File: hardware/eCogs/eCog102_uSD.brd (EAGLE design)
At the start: 47.5 x 28 mm, 7 parts

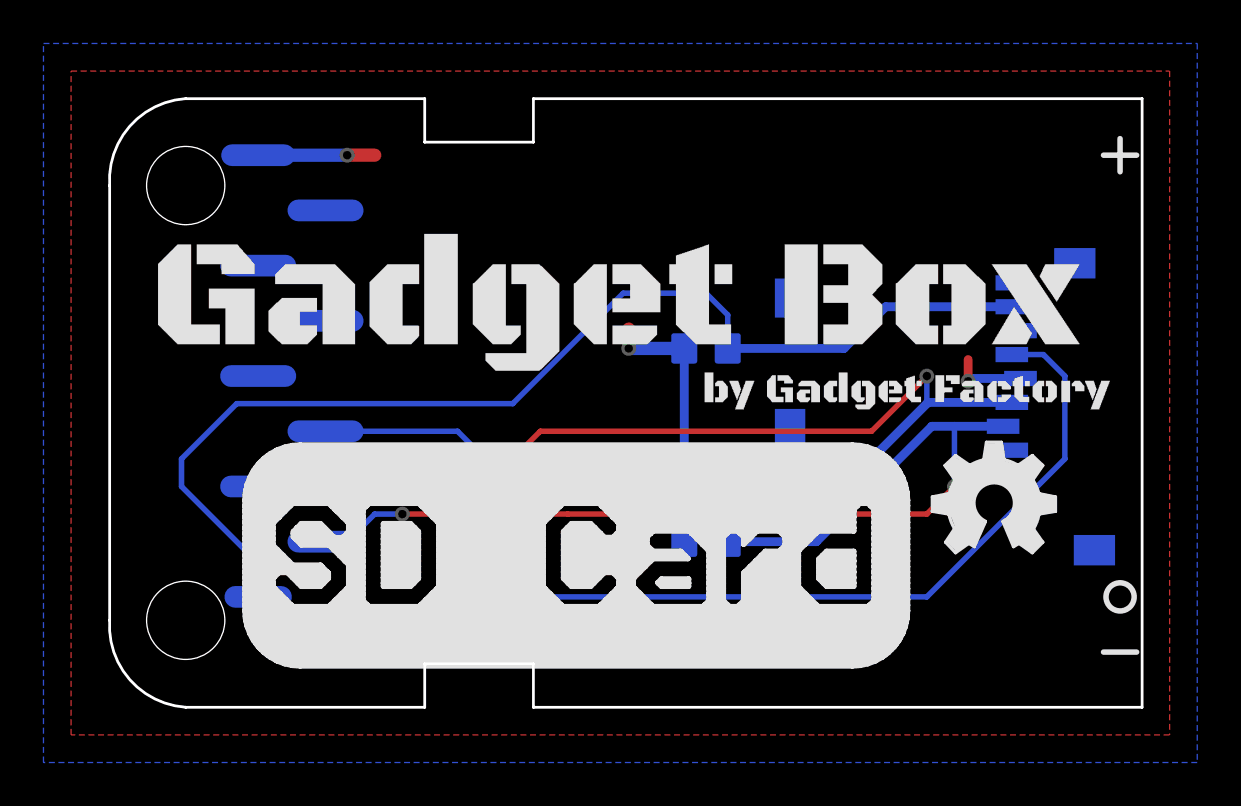
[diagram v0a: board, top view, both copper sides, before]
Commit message: Update eCogs to through hole
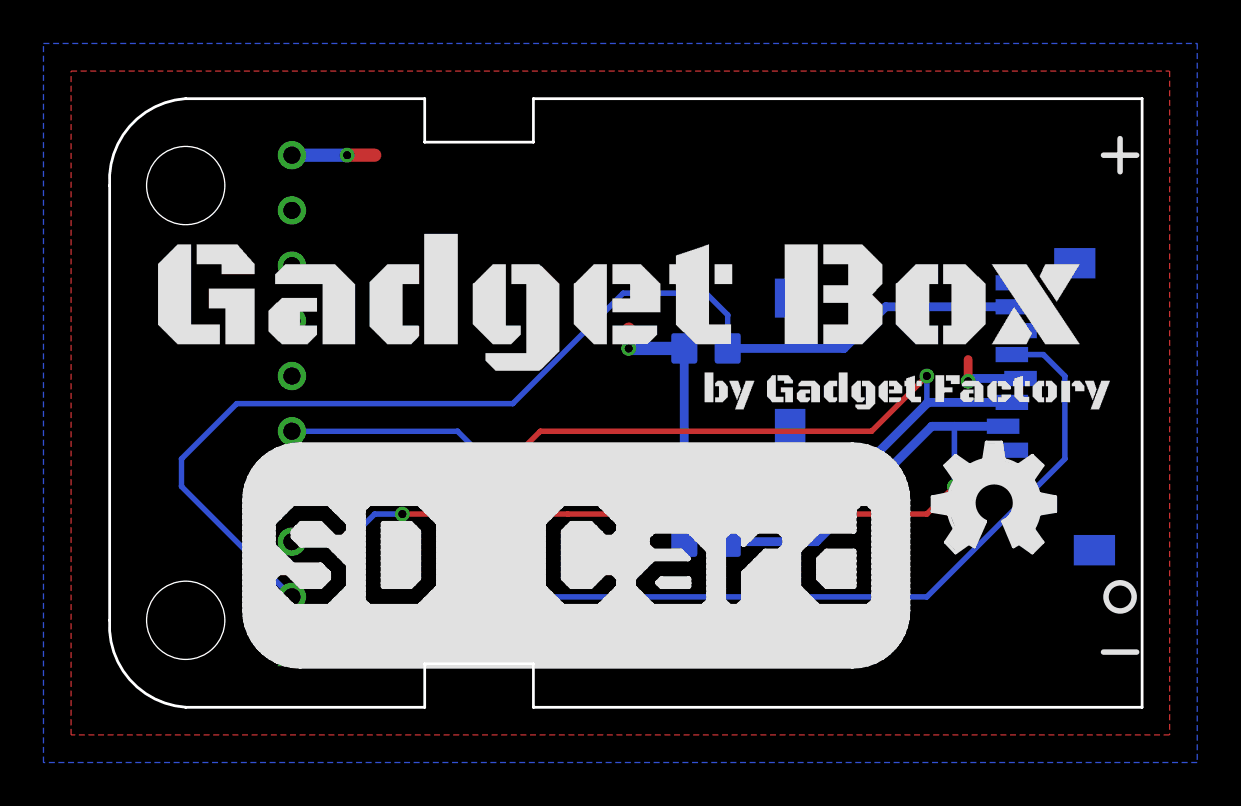
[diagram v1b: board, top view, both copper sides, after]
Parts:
- ECOG: value ECOG_BUSES_ROWECOG_BUSES_SMD -> ECOG_BUSES_ROWTHROUGHHOLE; device eCogs:ECOG_BUSES_SMD -> eCogs:ECOG_BUSES_TH
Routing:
- net SD_SCK: track 48.5 -> 47.0 mm
- net 3V3: track 21.2 -> 19.6 mm
- net SD_MOSI: track 46.8 -> 48.3 mm
- net SD_!CS: track 48.7 -> 50.2 mm
- net SD_MISO: track 52.3 -> 52.9 mm
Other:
- board text added: "ecog102 v2.1"
- board text removed: "ecog102 v2.0"
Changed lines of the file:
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@@
 <layer number="19" name="Unrouted" color="6" fill="1" visible="yes" active="yes"/>
 <layer number="20" name="Dimension" color="15" fill="1" visible="yes" active="yes"/>
-<layer number="21" name="tPlace" color="16" fill="1" visible="yes" active="yes"/>
+<layer number="21" name="tPlace" color="16" fill="1" visible="no" active="yes"/>
 <layer number="22" name="bPlace" color="14" fill="1" visible="yes" active="yes"/>
 <layer number="23" name="tOrigins" color="15" fill="1" visible="yes" active="yes"/>
@@
 <plain>
 <text x="35.179" y="24.765" size="0.8128" layer="22" font="vector" rot="MR0">ecog102.GadgetFactory.net</text>
-<text x="40.132" y="2.159" size="1.016" layer="22" font="vector" rot="MR0">ecog102 v2.0</text>
+<text x="40.132" y="2.159" size="1.016" layer="22" font="vector" rot="MR0">ecog102 v2.1</text>
 <text x="40.132" y="3.429" size="1.016" layer="22" font="vector" rot="MR0">uSD Card</text>
 <text x="40.132" y="4.699" size="1.016" layer="22" font="vector" rot="MR0">eCogs</text>
@@
 </autorouter>
 <elements>
-<element name="ECOG" library="eCogs" package="ECOG_BUSES_SMD" value="ECOG_BUSES_ROWECOG_BUSES_SMD" x="0" y="0" smashed="yes">
-<attribute name="DIGIKEY" value="S1013EC-10-ND" x="0" y="0" size="1.778" layer="27" display="off"/>
-</element>
+<element name="ECOG" library="eCogs" package="ECOG_BUSES_TH" value="ECOG_BUSES_ROWTHROUGHHOLE" x="0" y="0" smashed="yes"/>
 <element name="SD1" library="adafruit" package="MICROSD" value="MICROSD" x="31.369" y="20.828" smashed="yes" rot="MR270">
 <attribute name="NAME" x="36.579" y="13.318" size="1.27" layer="26" rot="MR270"/>
@@
 <wire x1="40" y1="15" x2="40" y2="16" width="0.4064" layer="1"/>
 <contactref element="ECOG" pad="3V3"/>
-<wire x1="7.337490625" y1="25.4" x2="11.43" y2="25.4" width="0.6096" layer="16"/>
+<wire x1="8.89" y1="25.4" x2="11.43" y2="25.4" width="0.6096" layer="16"/>
 <via x="11.43" y="25.4" extent="1-16" drill="0.381"/>
 <wire x1="11.43" y1="25.4" x2="12.7" y2="25.4" width="0.6096" layer="1"/>
@@
 <wire x1="29.21" y1="16.78" x2="28.94" y2="16.51" width="0.254" layer="16"/>
 <contactref element="ECOG" pad="SPI-MISO"/>
-<wire x1="7.337490625" y1="5.08" x2="7.337490625" y2="6.632509375" width="0.254" layer="16"/>
+<wire x1="8.89" y1="5.08" x2="7.337490625" y2="6.632509375" width="0.254" layer="16"/>
 <wire x1="7.337490625" y1="6.632509375" x2="3.81" y2="10.16" width="0.254" layer="16"/>
 <wire x1="3.81" y1="10.16" x2="3.81" y2="11.43" width="0.254" layer="16"/>
@@
 <wire x1="38.1" y1="15.24" x2="38.1" y2="13.97" width="0.254" layer="16"/>
 <contactref element="ECOG" pad="SPI-MOSI"/>
-<wire x1="10.436290625" y1="7.62" x2="11.43" y2="7.62" width="0.254" layer="16"/>
+<wire x1="8.89" y1="7.62" x2="11.43" y2="7.62" width="0.254" layer="16"/>
 <wire x1="11.43" y1="7.62" x2="12.7" y2="8.89" width="0.254" layer="16"/>
 <wire x1="12.7" y1="8.89" x2="13.97" y2="8.89" width="0.254" layer="16"/>
@@
 <wire x1="44.45" y1="15.24" x2="44.45" y2="11.43" width="0.254" layer="16"/>
 <contactref element="ECOG" pad="SPI-SCK"/>
-<wire x1="7.337490625" y1="10.16" x2="15.24" y2="10.16" width="0.254" layer="16"/>
+<wire x1="8.89" y1="10.16" x2="15.24" y2="10.16" width="0.254" layer="16"/>
 <wire x1="15.24" y1="10.16" x2="20.32" y2="5.08" width="0.254" layer="16"/>
 </signal>
@@
 <wire x1="39.37" y1="10.16" x2="39.37" y2="12.928" width="0.254" layer="16"/>
 <contactref element="ECOG" pad="SPI-CS"/>
-<wire x1="10.436290625" y1="12.7" x2="16.51" y2="12.7" width="0.254" layer="16"/>
+<wire x1="8.89" y1="12.7" x2="16.51" y2="12.7" width="0.254" layer="16"/>
 <wire x1="16.51" y1="12.7" x2="20.32" y2="8.89" width="0.254" layer="16"/>
 <via x="20.32" y="8.89" extent="1-16" drill="0.381"/>
